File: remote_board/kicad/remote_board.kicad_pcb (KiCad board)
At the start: 2 copper layers, 99 x 99 mm, 35 parts, among them U1 WeMos_D1_mini

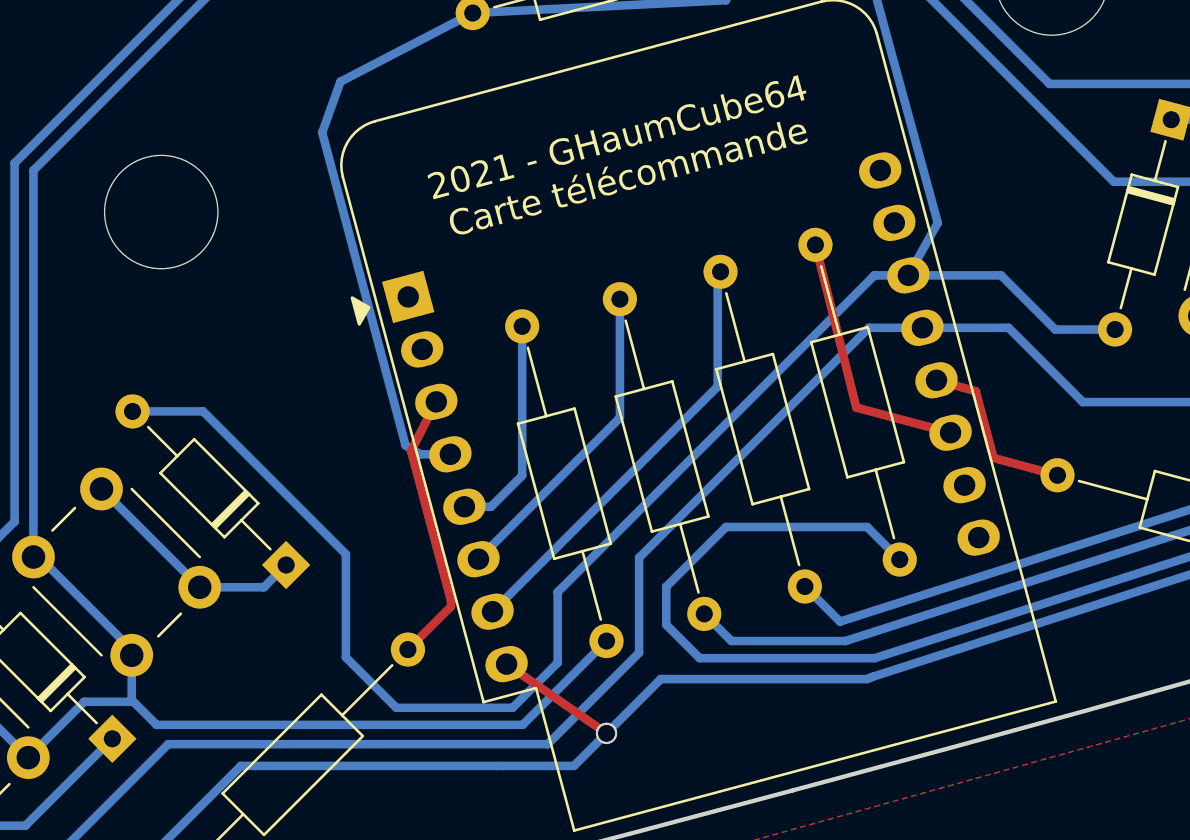
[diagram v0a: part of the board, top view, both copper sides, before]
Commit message: Update remote kicad schematic
Fixes from prototype:
- invert C1 & L2 (D8 always measures LOW level)
- invert leds on D3/D4 (for the builtin led to be on Z)
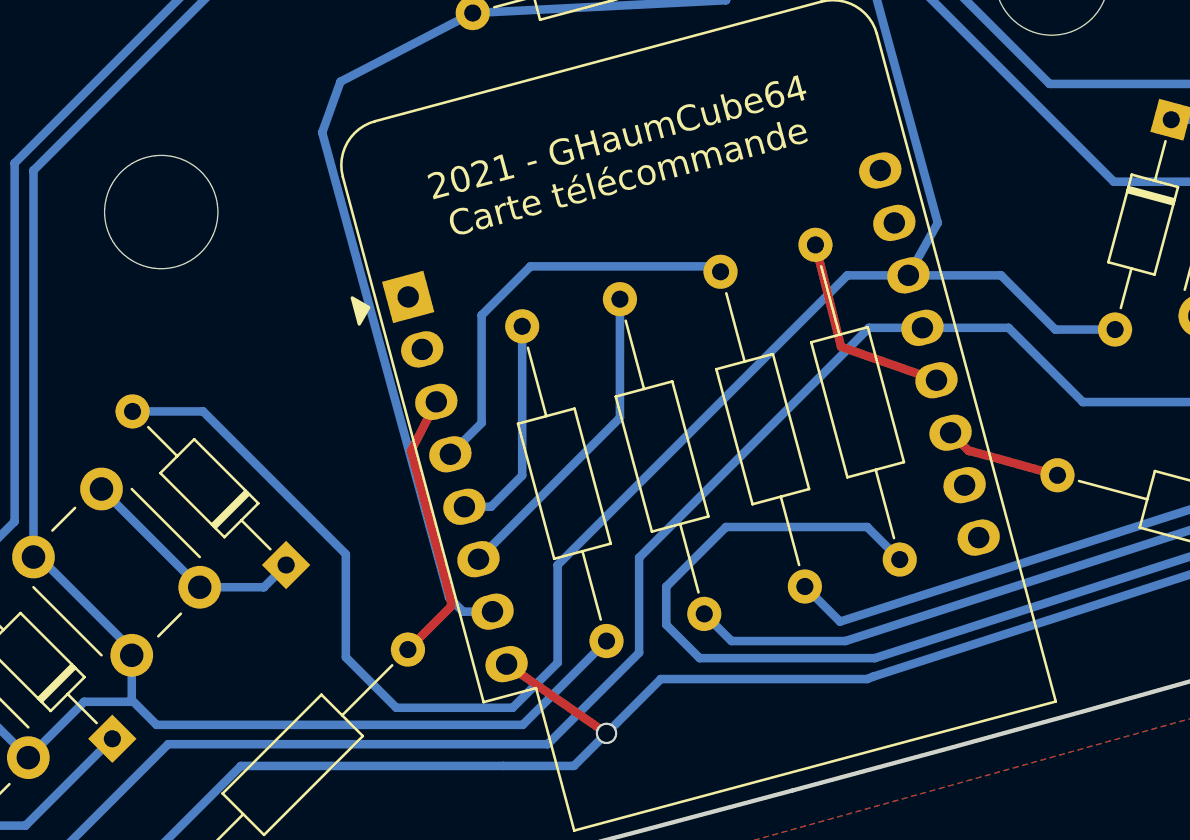
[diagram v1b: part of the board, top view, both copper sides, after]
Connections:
- U1 pad 11: Net-(R1-Pad2) -> Net-(R2-Pad2)
- U1 pad 12: Net-(R2-Pad2) -> Net-(R1-Pad2)
- U1 pad 4: /L2 -> /C1
- U1 pad 7: /C1 -> /L2
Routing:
- net /L2: track 50.6 -> 57.7 mm
- net Net-(R1-Pad2): track 12.4 -> 9.65 mm
- net Net-(R2-Pad2): track 8.23 -> 5.51 mm
- net /C1: track 20.2 -> 19.3 mm
- net /L1: track 108.1 -> 108.8 mm

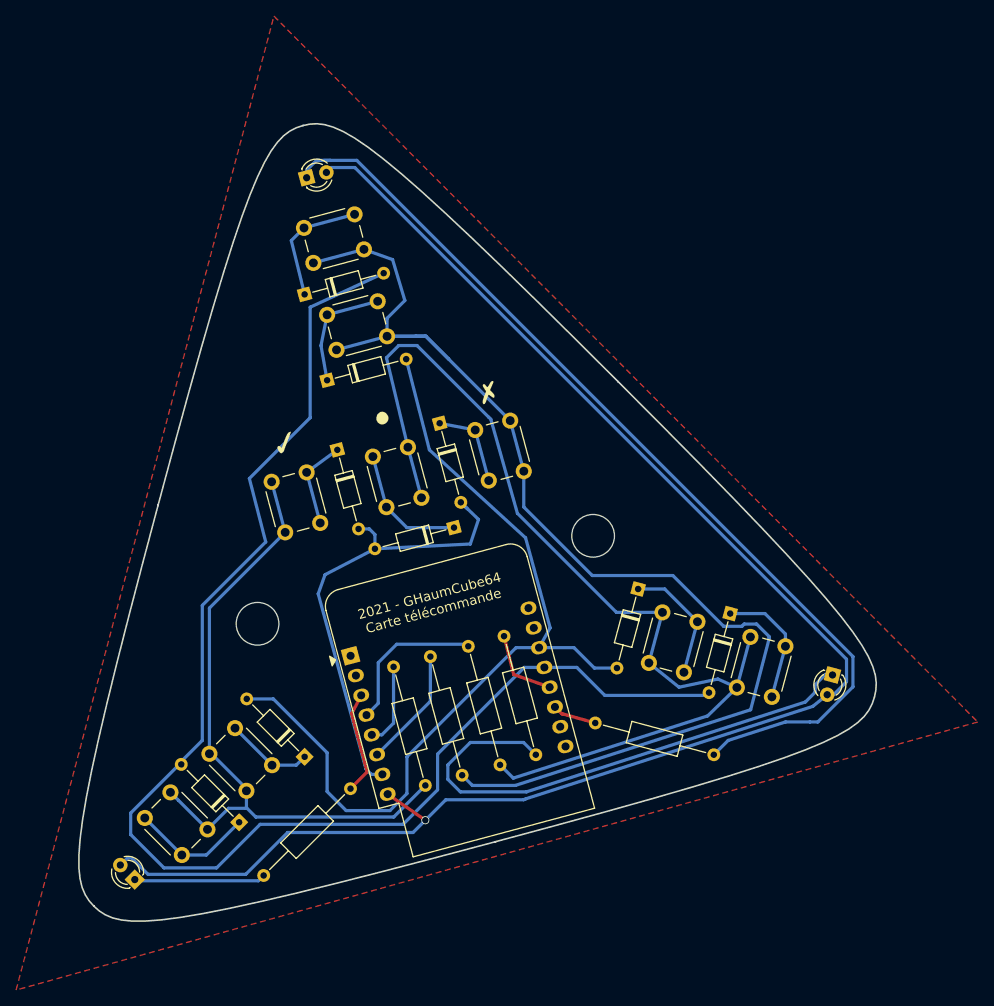
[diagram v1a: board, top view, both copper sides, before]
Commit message: Change button footprint in remote board
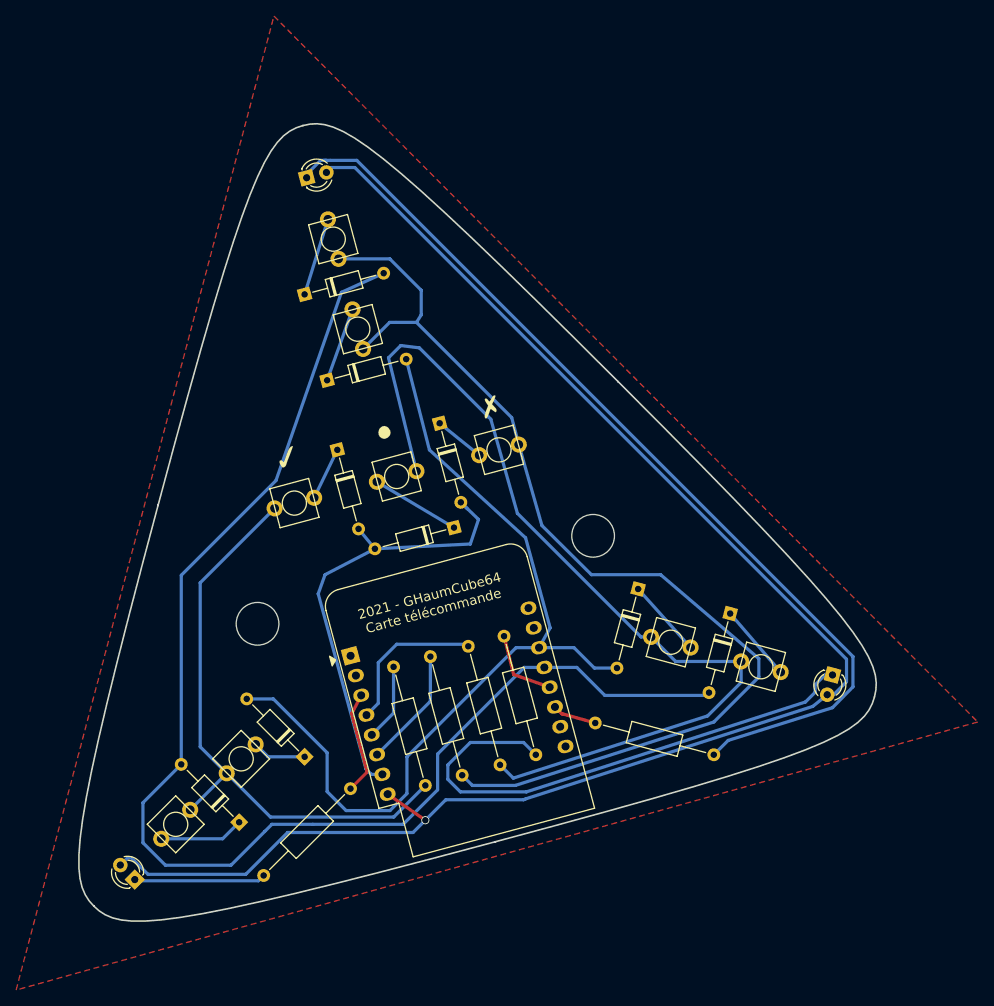
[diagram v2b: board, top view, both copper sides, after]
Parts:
- S0, S1, S2, S3, S4, S5, S6, S7, S8: footprint Button_Switch_THT:SW_PUSH_6mm -> custom_footprints:SW_PUSH_5mm_2pins
- moved S5 4.20 mm to (135.9, 76.7), turned to 285 degrees
- moved S4 4.17 mm to (174.8, 115.6), turned to 165 degrees
- moved S6 4.10 mm to (128.0, 98.3), turned to 195 degrees
- moved S7 4.02 mm to (140.7, 95.0), turned to 15 degrees
- moved S8 4.02 mm to (153.4, 91.7), turned to 15 degrees
- moved S1 3.97 mm to (185.9, 118.6), turned to 165 degrees
- moved S2 3.89 mm to (132.8, 65.5), turned to 285 degrees
- moved S0 3.89 mm to (113.3, 138.2), turned to 45 degrees
- moved S3 3.89 mm to (121.4, 130.0), turned to 225 degrees
- moved G*** 1.80 mm to (139.7, 89.2)
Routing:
- net Net-(R5-Pad1): track 151.9 -> 131.1 mm
- net Net-(R4-Pad1): track 128.6 -> 115.2 mm
- net Net-(R3-Pad1): track 83.2 -> 73.0 mm
- net Net-(D1-Pad1): track 15.9 -> 9.59 mm
- net /L0: track 174.0 -> 168.1 mm
- net Net-(D2-Pad1): track 15.6 -> 9.75 mm
- net Net-(D4-Pad1): track 15.5 -> 9.76 mm
- net Net-(D5-Pad1): track 14.8 -> 9.35 mm
- net Net-(D6-Pad1): track 11.6 -> 6.61 mm
- net Net-(D7-Pad1): track 15.9 -> 11.1 mm
- net Net-(D0-Pad1): track 15.3 -> 10.5 mm
- net Net-(D8-Pad1): track 11.0 -> 6.52 mm
- net Net-(D3-Pad1): track 11.0 -> 6.72 mm
- net Net-(L2-Pad1): track 120.2 -> 119.0 mm
- net /L2: track 57.7 -> 56.8 mm
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
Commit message: Change component placement in remote board
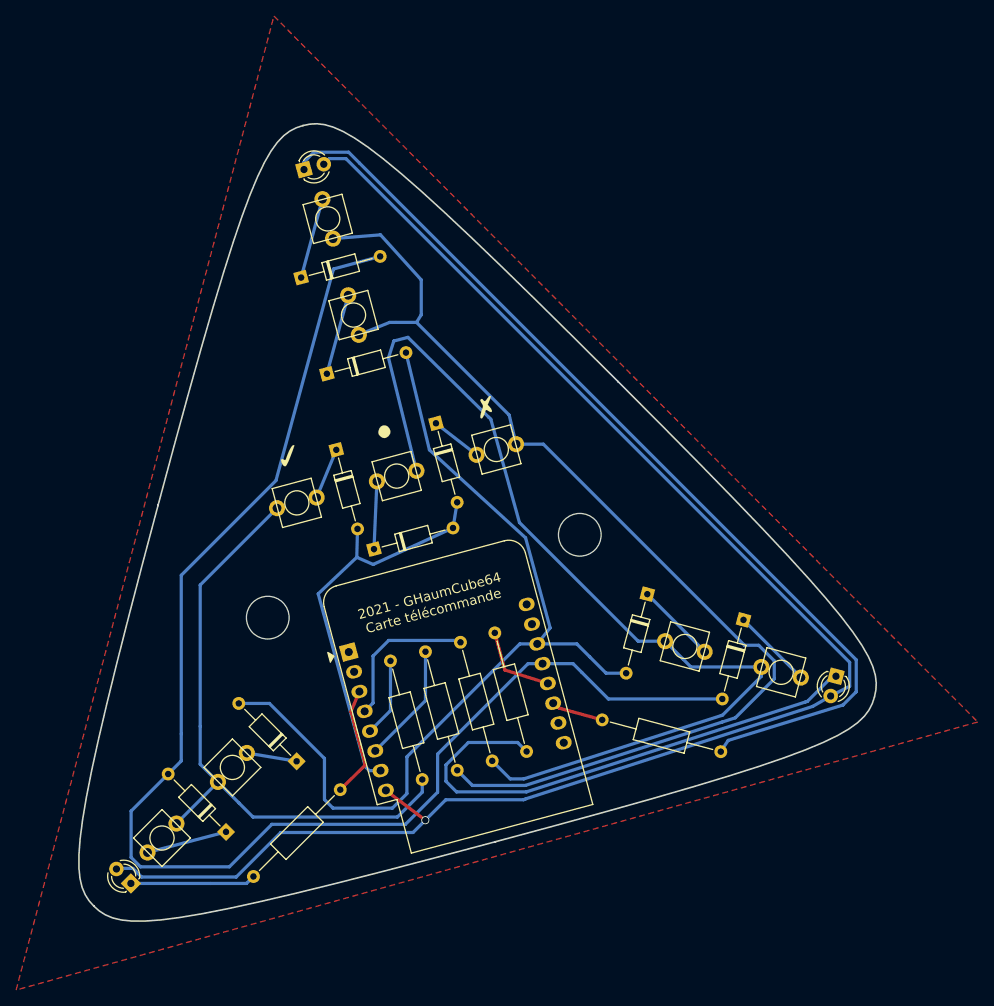
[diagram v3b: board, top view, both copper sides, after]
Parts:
- removed the G*** at (139.7, 89.2)
- removed the REF** at (103.1, 148.3)
- added G***: LOGO, g, F.Cu at (139.5, 89.5)
- added REF**: spot, spot, F.Cu at (101.1, 150.3)
- moved D7 10.3 mm to (137.9, 104.0), turned to 15 degrees
- moved S1 2.61 mm to (188.4, 119.3)
- moved S2 2.61 mm to (132.2, 63.0)
- moved S0 2.41 mm to (111.6, 139.9)
- moved D2 2.13 mm to (128.9, 70.3)
- moved D0 2.02 mm to (119.5, 139.1)
- moved G*** 1.88 mm to (135.5, 103.0)
- moved S5 1.83 mm to (135.4, 75.0)
- moved D1 1.83 mm to (183.8, 112.8)
- moved S4 1.82 mm to (176.5, 116.1)
- moved G*** 1.82 mm to (116.0, 112.0)
- moved H2 1.66 mm to (163.4, 102.2)
- moved S3 1.53 mm to (120.3, 131.1)
- moved H1 1.48 mm to (124.7, 112.5)
- moved D4 1.31 mm to (171.8, 109.6)
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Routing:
- net /L0: track 168.1 -> 176.4 mm
- net Net-(R4-Pad1): track 115.2 -> 122.4 mm
- net /L2: track 56.8 -> 50.8 mm
- net Net-(R5-Pad1): track 131.1 -> 135.2 mm
- net Net-(R3-Pad1): track 73.0 -> 76.2 mm
- net /L1: track 108.8 -> 111.8 mm
- net Net-(D7-Pad1): track 11.1 -> 8.42 mm
- net Net-(L0-Pad2): track 196.8 -> 198.5 mm
- net Net-(R2-Pad2): track 5.51 -> 6.54 mm
- net Net-(R0-Pad2): track 13.0 -> 13.9 mm
- net Net-(L1-Pad1): track 66.6 -> 65.8 mm
- net Net-(L0-Pad1): track 16.3 -> 15.6 mm
- net Net-(D5-Pad1): track 9.35 -> 10.1 mm
- net Net-(R1-Pad2): track 9.65 -> 10.4 mm
- net Net-(D1-Pad1): track 9.59 -> 10.1 mm

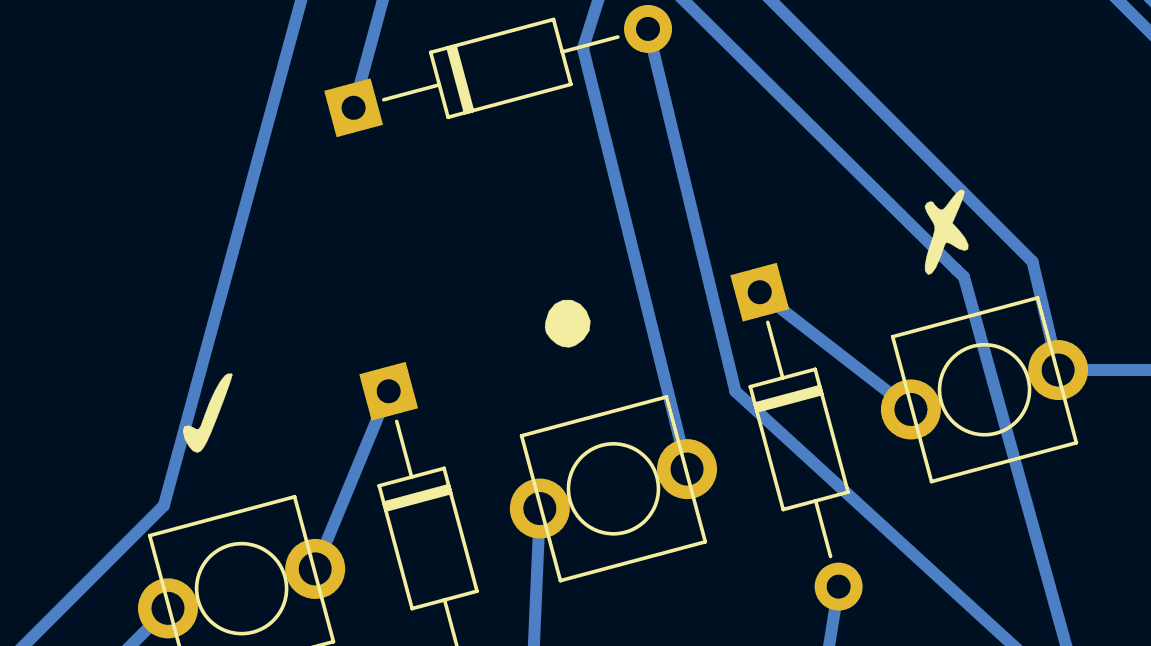
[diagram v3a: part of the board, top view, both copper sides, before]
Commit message: Change meaning of left/right buttons in remote board
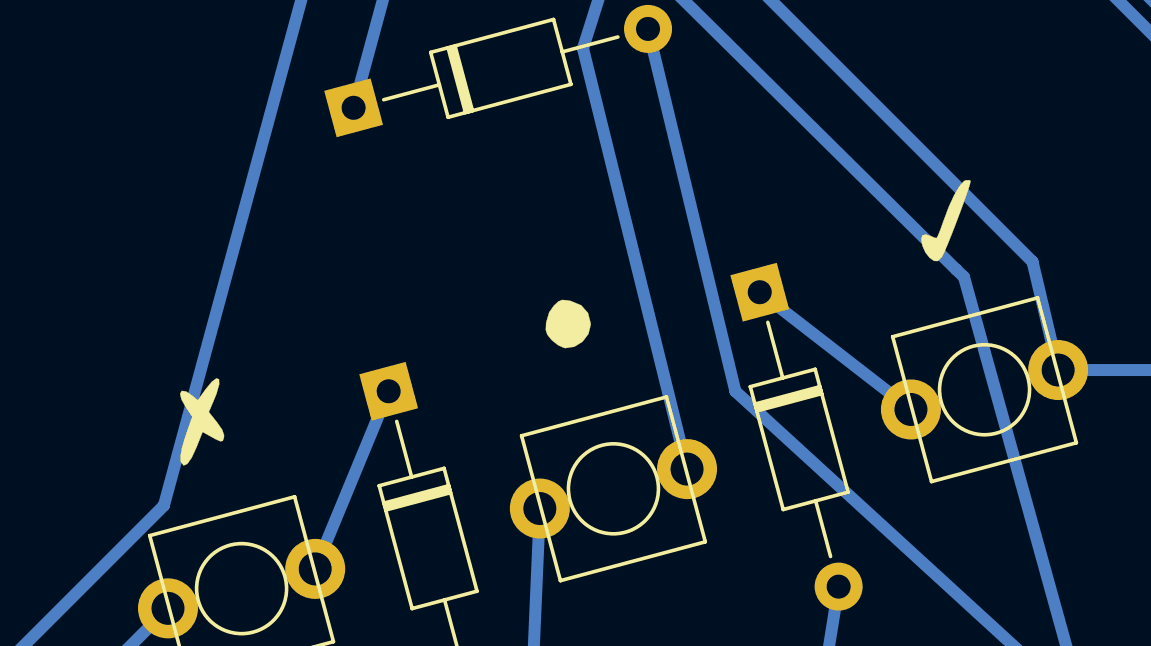
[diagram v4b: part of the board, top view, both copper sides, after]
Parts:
- moved G*** 0.13 mm to (139.4, 89.4)
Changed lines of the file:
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@@
   )
   (module g (layer F.Cu)
-    (at 139.4968 89.4842 15)
+    (at 139.4206 89.3826 15)
     (fp_text reference G*** (at 0 0 15) (layer F.SilkS) hide
       (effects (font (size 1.524 1.524) (thickness 0.3)))
@@
       (effects (font (size 1.524 1.524) (thickness 0.3)))
     )
-    (fp_poly (pts (xy 13.627488 -0.978666) (xy 13.631333 -0.937397) (xy 13.582256 -0.83987) (xy 13.454492 -0.654571)
-      (xy 13.301345 -0.454339) (xy 12.971356 -0.039891) (xy 13.128463 0.255221) (xy 13.256565 0.559831)
-      (xy 13.292721 0.792199) (xy 13.247947 0.931794) (xy 13.133257 0.958083) (xy 12.959667 0.850534)
-      (xy 12.862881 0.750245) (xy 12.702786 0.581683) (xy 12.606035 0.534738) (xy 12.538298 0.592667)
-      (xy 12.279038 0.979398) (xy 12.053636 1.251188) (xy 11.872779 1.400024) (xy 11.747157 1.417895)
-      (xy 11.687457 1.296789) (xy 11.684 1.233018) (xy 11.730531 1.064886) (xy 11.853298 0.812224)
-      (xy 12.027064 0.526062) (xy 12.051545 0.489849) (xy 12.235728 0.215604) (xy 12.337367 0.033255)
-      (xy 12.370187 -0.104608) (xy 12.347914 -0.245392) (xy 12.303578 -0.380651) (xy 12.240139 -0.615414)
-      (xy 12.22349 -0.791975) (xy 12.22971 -0.822815) (xy 12.318414 -0.906319) (xy 12.445173 -0.93057)
-      (xy 12.526951 -0.884523) (xy 12.530667 -0.862849) (xy 12.575789 -0.745946) (xy 12.640784 -0.64377)
-      (xy 12.713783 -0.566643) (xy 12.798501 -0.564899) (xy 12.935744 -0.651734) (xy 13.114493 -0.796948)
-      (xy 13.375345 -0.985957) (xy 13.548997 -1.047251) (xy 13.627488 -0.978666)) (layer F.SilkS) (width 0.01))
-    (fp_poly (pts (xy -11.541434 -1.414409) (xy -11.514667 -1.383412) (xy -11.561156 -1.295647) (xy -11.686841 -1.102154)
-      (xy -11.871043 -0.83395) (xy -12.036726 -0.600245) (xy -12.408749 -0.086579) (xy -12.699177 0.300017)
-      (xy -12.921808 0.572377) (xy -13.090442 0.743337) (xy -13.218876 0.825734) (xy -13.320909 0.832401)
-      (xy -13.41034 0.776176) (xy -13.459244 0.722987) (xy -13.537479 0.560584) (xy -13.598573 0.319039)
-      (xy -13.606058 0.270004) (xy -13.600514 0.012146) (xy -13.513506 -0.120192) (xy -13.366431 -0.111681)
-      (xy -13.22738 -0.001296) (xy -13.140154 0.080026) (xy -13.06608 0.08552) (xy -12.972303 -0.005209)
-      (xy -12.825969 -0.212558) (xy -12.782274 -0.277622) (xy -12.500099 -0.66963) (xy -12.221524 -1.005065)
-      (xy -11.969602 -1.259777) (xy -11.76739 -1.409616) (xy -11.673217 -1.439333) (xy -11.541434 -1.414409)) (layer F.SilkS) (width 0.01))
-    (fp_poly (pts (xy 0.049785 -0.847257) (xy 0.287164 -0.64221) (xy 0.427265 -0.369086) (xy 0.469823 -0.013248)
-      (xy 0.356314 0.2896) (xy 0.096139 0.517119) (xy 0.042893 0.544393) (xy -0.221948 0.64817)
-      (xy -0.42737 0.657462) (xy -0.651717 0.575983) (xy -0.813692 0.439658) (xy -0.96007 0.227345)
-      (xy -0.971681 0.203892) (xy -1.054449 -0.012986) (xy -1.047738 -0.192587) (xy -0.985075 -0.366757)
-      (xy -0.783746 -0.68187) (xy -0.520764 -0.867029) (xy -0.231223 -0.922178) (xy 0.049785 -0.847257)) (layer F.SilkS) (width 0.01))
+    (fp_poly (pts (xy -0.038467 -0.753214) (xy 0.058916 -0.705843) (xy 0.355937 -0.478814) (xy 0.508053 -0.174463)
+      (xy 0.505071 0.185204) (xy 0.493439 0.232392) (xy 0.341805 0.506268) (xy 0.087244 0.702929)
+      (xy -0.217777 0.796924) (xy -0.520789 0.7628) (xy -0.563122 0.744917) (xy -0.725619 0.613388)
+      (xy -0.880732 0.40628) (xy -0.895326 0.380247) (xy -0.9868 0.179129) (xy -0.995758 0.012625)
+      (xy -0.92638 -0.211151) (xy -0.922669 -0.220927) (xy -0.737115 -0.525163) (xy -0.527737 -0.702383)
+      (xy -0.34512 -0.798728) (xy -0.209346 -0.815511) (xy -0.038467 -0.753214)) (layer F.SilkS) (width 0.01))
+    (fp_poly (pts (xy 13.941595 -1.157286) (xy 13.96762 -1.121834) (xy 13.918814 -1.025714) (xy 13.789025 -0.823983)
+      (xy 13.59943 -0.546076) (xy 13.371205 -0.221426) (xy 13.125529 0.120533) (xy 12.883577 0.450366)
+      (xy 12.666528 0.73864) (xy 12.495557 0.95592) (xy 12.391843 1.072773) (xy 12.38382 1.0795)
+      (xy 12.221649 1.172962) (xy 12.100298 1.136728) (xy 11.985134 0.997161) (xy 11.895304 0.791575)
+      (xy 11.85705 0.546288) (xy 11.873926 0.328375) (xy 11.943335 0.208369) (xy 12.067953 0.215127)
+      (xy 12.182835 0.288039) (xy 12.315554 0.393072) (xy 12.377179 0.423333) (xy 12.443082 0.358305)
+      (xy 12.572284 0.188013) (xy 12.732998 -0.045025) (xy 13.031863 -0.465262) (xy 13.31457 -0.807185)
+      (xy 13.561705 -1.050249) (xy 13.753851 -1.173906) (xy 13.810519 -1.185334) (xy 13.941595 -1.157286)) (layer F.SilkS) (width 0.01))
+    (fp_poly (pts (xy -11.943036 -1.221896) (xy -11.981122 -1.058644) (xy -12.138653 -0.7932) (xy -12.245318 -0.649334)
+      (xy -12.552635 -0.254879) (xy -12.37939 0.145342) (xy -12.276153 0.430566) (xy -12.262391 0.621677)
+      (xy -12.291554 0.705149) (xy -12.353611 0.79365) (xy -12.429153 0.791283) (xy -12.560568 0.685516)
+      (xy -12.651386 0.598754) (xy -12.925809 0.332772) (xy -13.258931 0.779354) (xy -13.503201 1.072278)
+      (xy -13.694475 1.230235) (xy -13.823923 1.249127) (xy -13.882711 1.12486) (xy -13.885333 1.069893)
+      (xy -13.83874 0.899974) (xy -13.715545 0.64481) (xy -13.540626 0.354711) (xy -13.507003 0.304762)
+      (xy -13.128673 -0.247846) (xy -13.249774 -0.591081) (xy -13.32605 -0.890949) (xy -13.320026 -1.08941)
+      (xy -13.244508 -1.169521) (xy -13.112305 -1.114338) (xy -12.972132 -0.958379) (xy -12.806806 -0.731423)
+      (xy -12.480112 -1.000712) (xy -12.199065 -1.202707) (xy -12.017862 -1.273175) (xy -11.943036 -1.221896)) (layer F.SilkS) (width 0.01))
   )
   (module backsilk (layer B.Cu)
